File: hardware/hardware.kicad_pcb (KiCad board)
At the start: 2 copper layers, 91.4 x 91.4 mm, 99 parts, among them J1 DB25_Female, J2 USB_B_Micro, J3 RJ45_Bel_SI-60062-F-68net, U1 MIC5319, U11 ENC28J60x-SO, U12 74LVC14, U2 74LVTH126, U3 74LVTH126, U4 LM1117-ADJ, U5 74LVTH126, U6 74LVTH126, U7 STM32F072R8Tx, U8 74LVC245, Y1 8MHz, Y2 25MHz

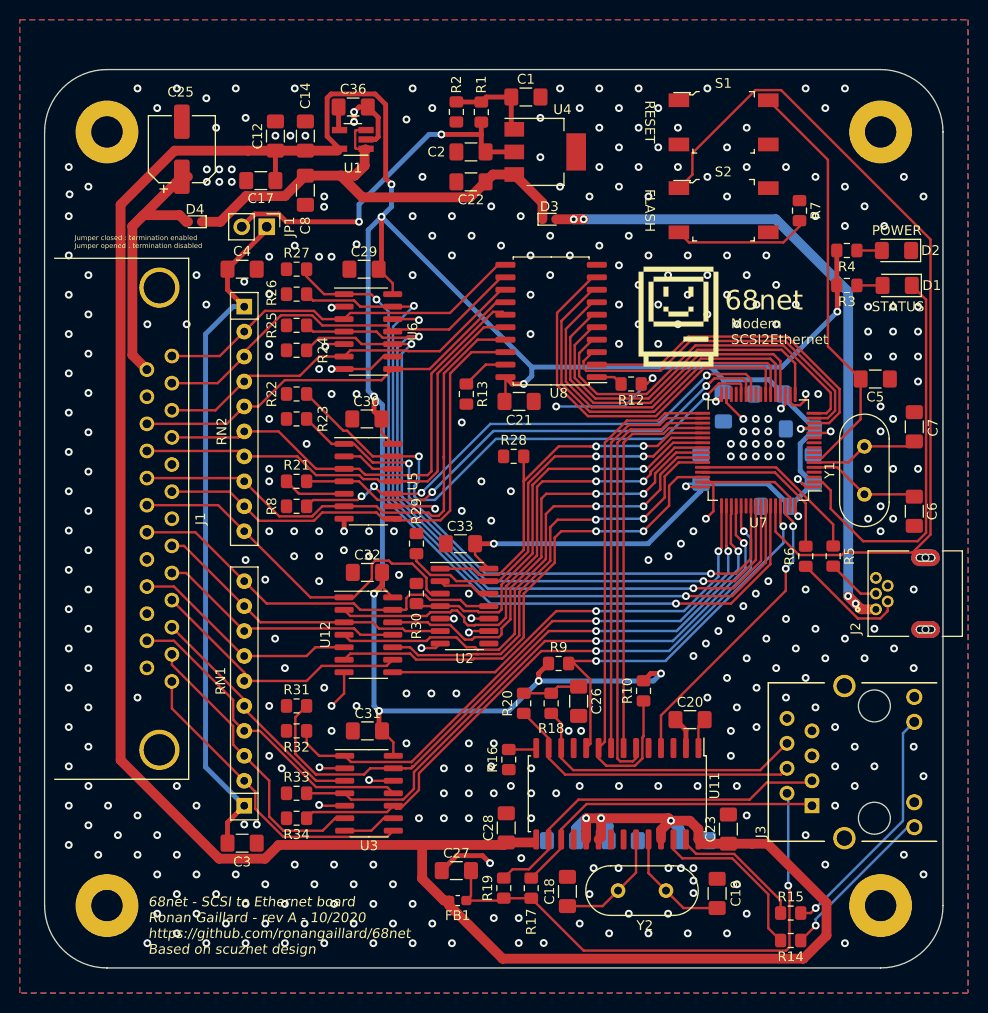
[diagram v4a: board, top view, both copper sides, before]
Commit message: feat: add double DB25 connector
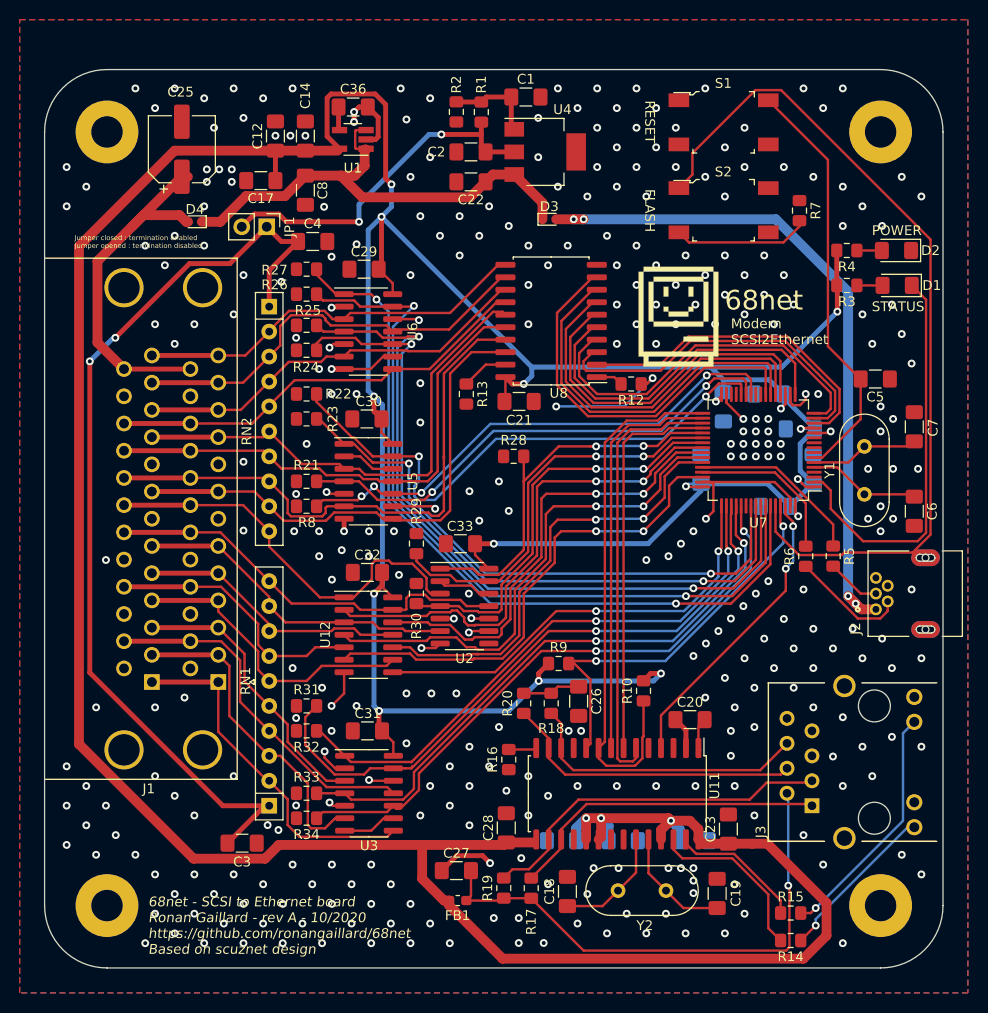
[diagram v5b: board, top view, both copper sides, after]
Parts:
- J1: footprint kicad-footprints-perso:D25S13A -> kicad-footprints-perso:DSUB-25_Female_Horizontal_Double
- moved J1 20.3 mm to (20.3, 66.0), turned to 270 degrees
- moved C4 7.72 mm to (47.6, 37.8)
- moved RN1 2.54 mm to (43.2, 95.2)
- moved RN2 2.54 mm to (43.2, 44.5)
- moved R21 1.02 mm to (47.0, 62.2)
- moved R22 1.02 mm to (47.0, 53.3)
- moved R23 1.02 mm to (47.0, 55.9)
- moved R24 1.02 mm to (47.0, 48.9)
- moved R25 1.02 mm to (47.0, 46.4)
- moved R26 1.02 mm to (47.0, 43.2)
- moved R27 1.02 mm to (47.0, 40.6)
- moved R31 1.02 mm to (47.0, 85.1)
- moved R32 1.02 mm to (47.0, 87.6)
- moved R33 1.02 mm to (47.0, 94.0)
- moved R34 1.02 mm to (47.0, 96.5)
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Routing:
- net Net-(C3-Pad1): track 69.7 -> 97.0 mm, vias 0 -> 2
- net /TPWR: track 29.4 -> 38.0 mm
- net GND: track 112.9 -> 107.6 mm, vias 386 -> 347
- net +3V3: track 514.5 -> 519.6 mm
- net /IO: track 24.3 -> 28.8 mm
- net /CD: track 32.7 -> 36.9 mm
- net /REQ: track 32.0 -> 35.9 mm
- net /ATN: track 23.4 -> 26.9 mm
- net /DB6: track 40.0 -> 43.4 mm
- net /DB1: track 55.2 -> 58.6 mm
- net /MSG: track 29.4 -> 32.8 mm
- net /RST: track 27.3 -> 30.6 mm
- net /DBP: track 38.3 -> 41.5 mm
- net /ACK: track 24.9 -> 27.7 mm
- net /BSY: track 30.9 -> 33.5 mm
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
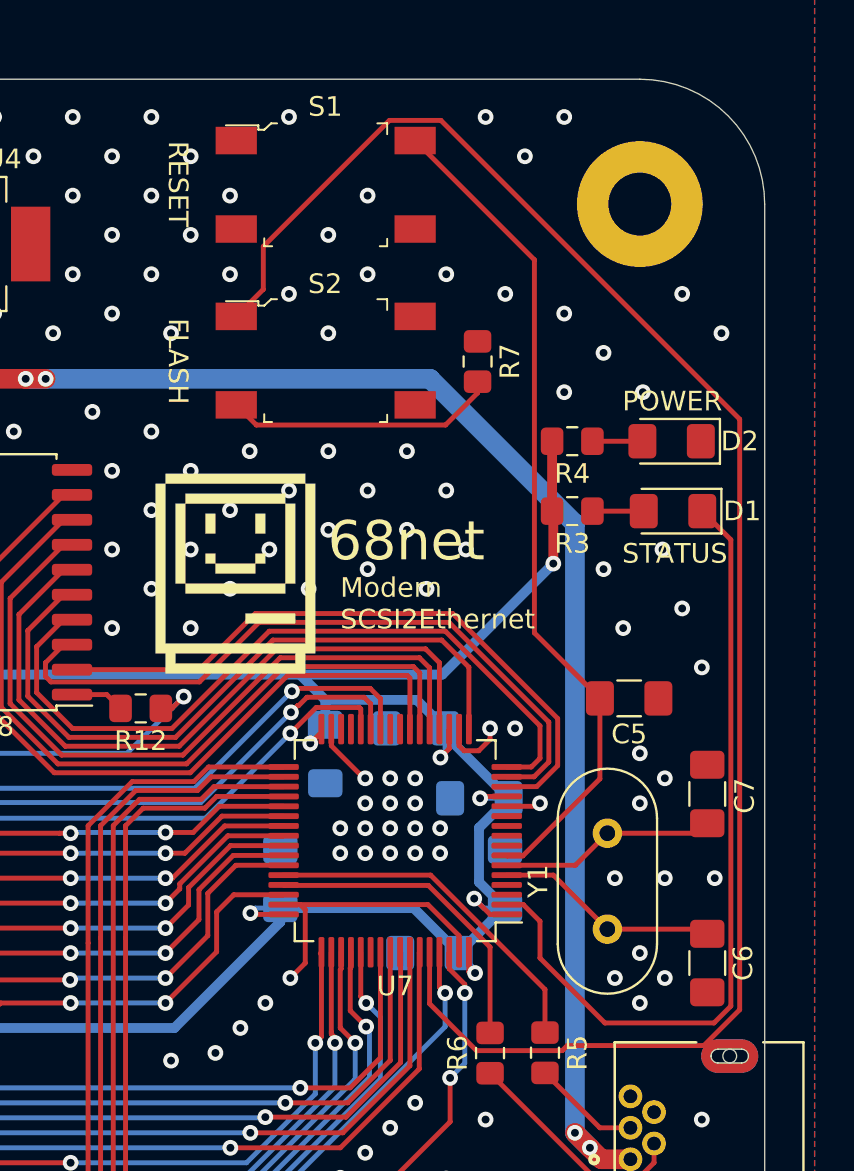
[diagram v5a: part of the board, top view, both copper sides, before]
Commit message: feat: add connectors for external LEDs
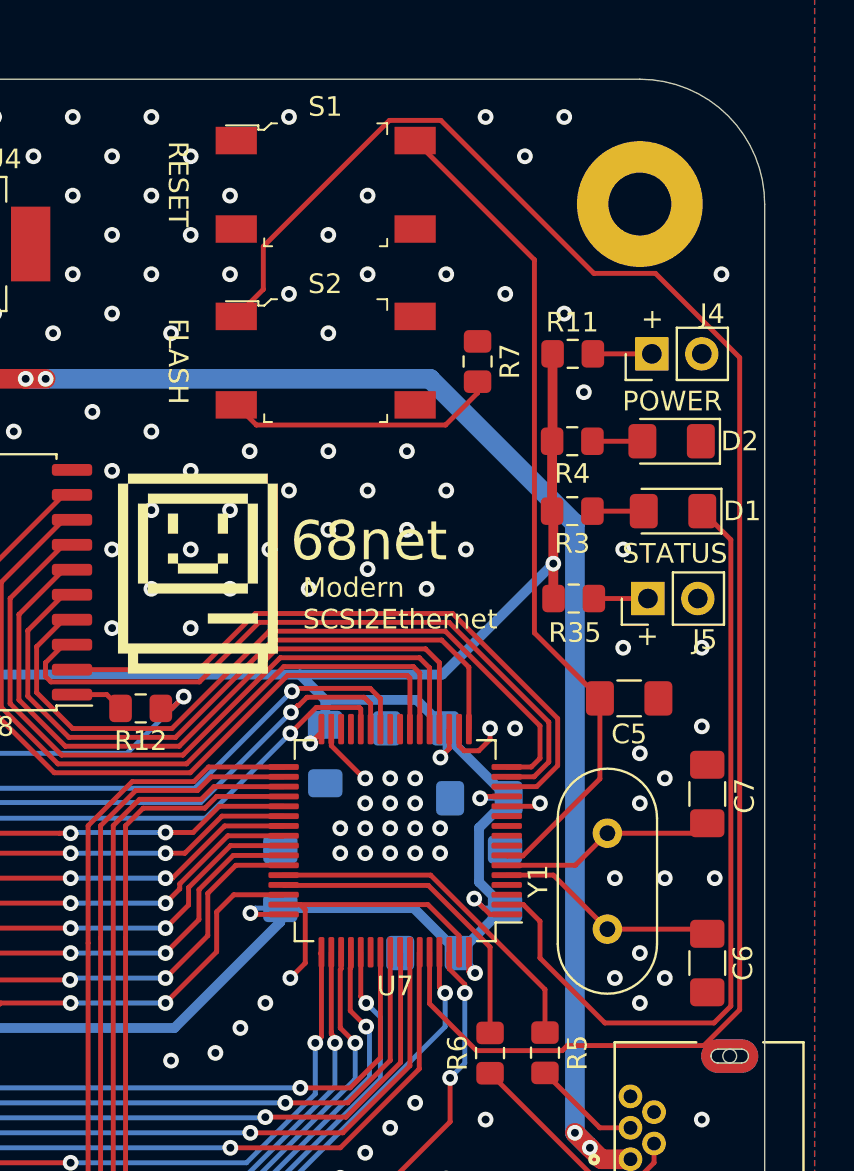
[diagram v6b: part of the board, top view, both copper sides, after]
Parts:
- added J4: Conn_01x02_Male, Connector_PinHeader_2.54mm:PinHeader_1x02_P2.54mm_Vertical, F.Cu at (106.0, 34.3)
- added J5: Conn_01x02_Male, Connector_PinHeader_2.54mm:PinHeader_1x02_P2.54mm_Vertical, F.Cu at (105.8, 46.7)
- added R11: 100, Resistor_SMD:R_0805_2012Metric_Pad1.15x1.40mm_HandSolder, F.Cu at (102.0, 34.3)
- added R35: 100, Resistor_SMD:R_0805_2012Metric_Pad1.15x1.40mm_HandSolder, F.Cu at (102.0, 46.7)
- R3, R4: value 165 -> 100
- moved G*** 1.91 mm to (82.9, 45.5)
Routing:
- net +3V3: track 519.6 -> 525.8 mm
- net Net-(J4-Pad1): track 0.00 -> 3.00 mm
- net Net-(J5-Pad1): track 0.00 -> 2.89 mm
- net /BOOT0: track 87.6 -> 89.4 mm
- net GND: vias 347 -> 343
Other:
- board text added: "+"

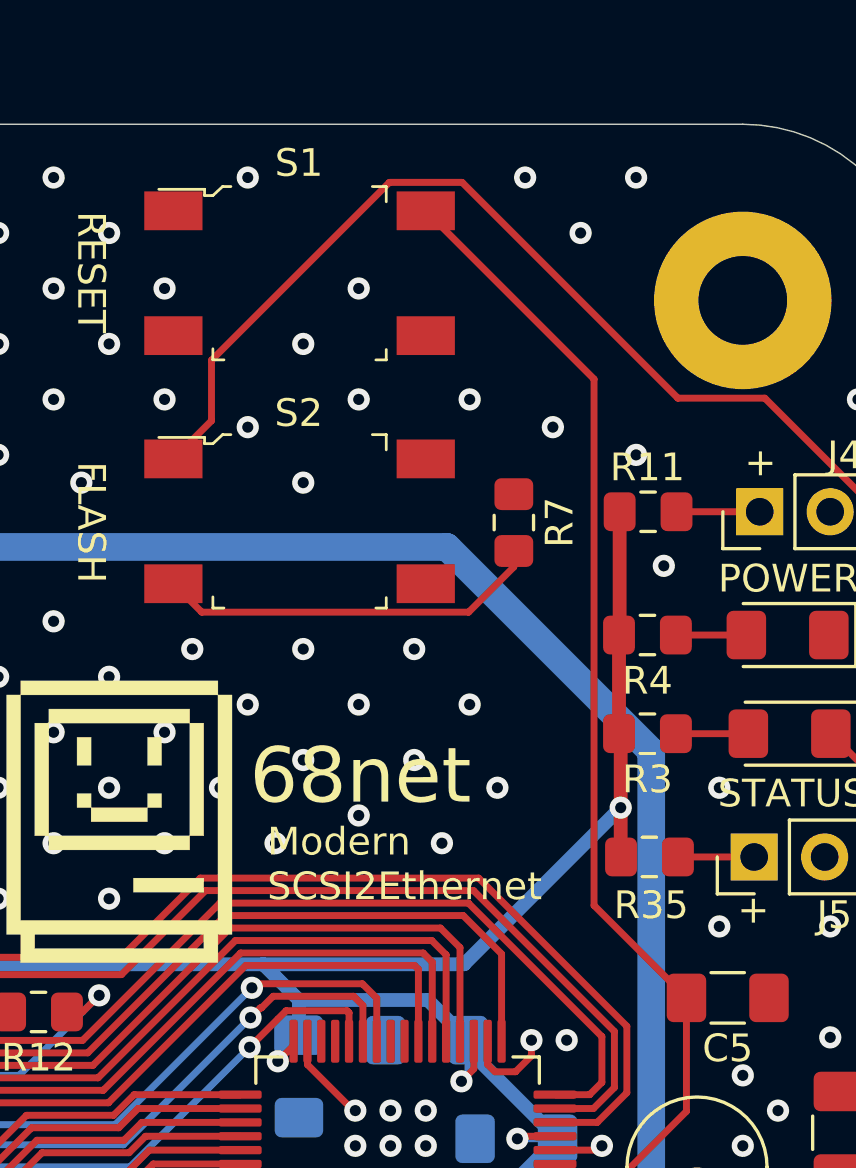
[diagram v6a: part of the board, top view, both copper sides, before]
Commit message: fix: boot and rst signal badly pulled up/down
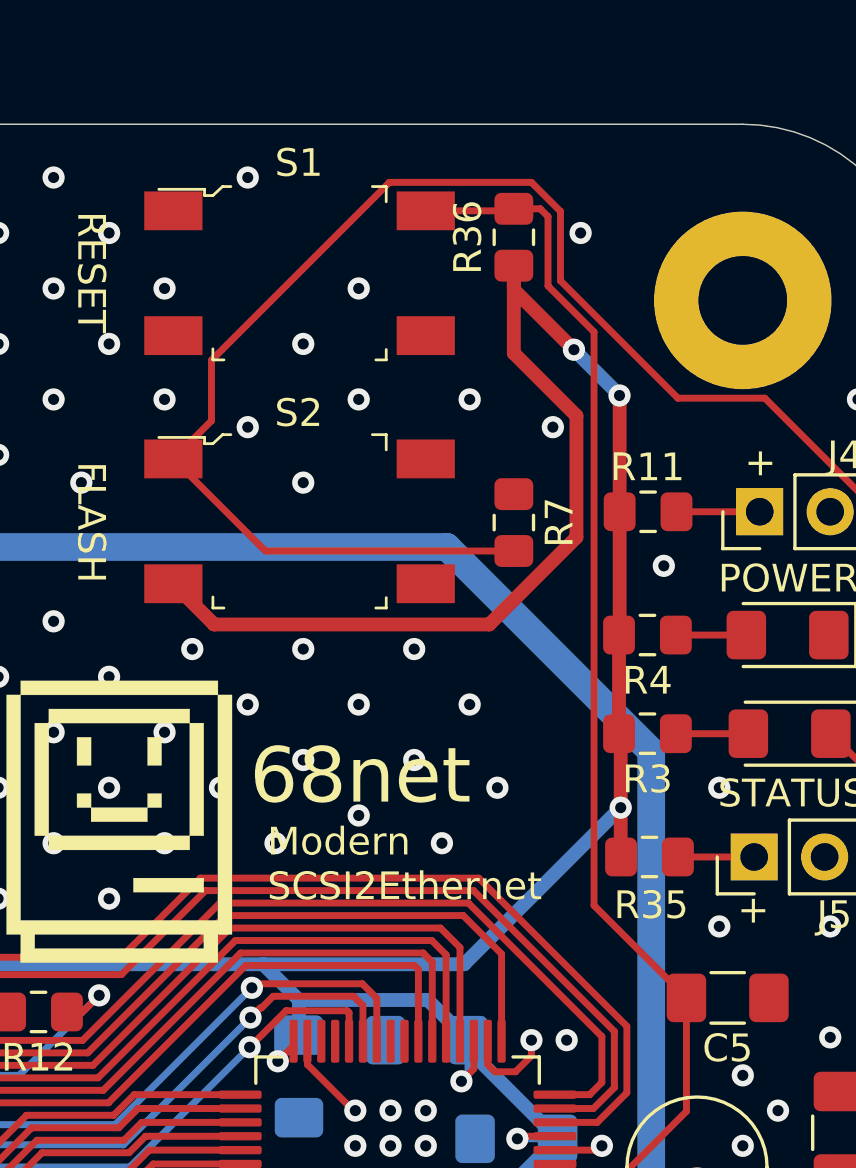
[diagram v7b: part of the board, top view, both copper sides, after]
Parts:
- added R36: 10k, Resistor_SMD:R_0805_2012Metric_Pad1.15x1.40mm_HandSolder, F.Cu at (97.2, 24.4)
- S1: value PTS645SM43SMTR92_LFS -> SWITCH
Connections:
- R7 pad 1: Net-(R7-Pad1) -> /BOOT0
- S2 pad 3: Net-(R7-Pad1) -> +3V3
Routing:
- net +3V3: track 525.8 -> 563.4 mm, vias 19 -> 21
- net /BOOT0: track 89.4 -> 104.5 mm
- net Net-(R7-Pad1): track 13.9 -> 0.00 mm
- net /NRST: track 42.7 -> 45.3 mm
- net GND: vias 343 -> 340
